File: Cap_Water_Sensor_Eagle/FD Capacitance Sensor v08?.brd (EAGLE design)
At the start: 35.1 x 27.6 mm, 17 parts, among them U1 NTS4101PT1, U2 TLC555CD

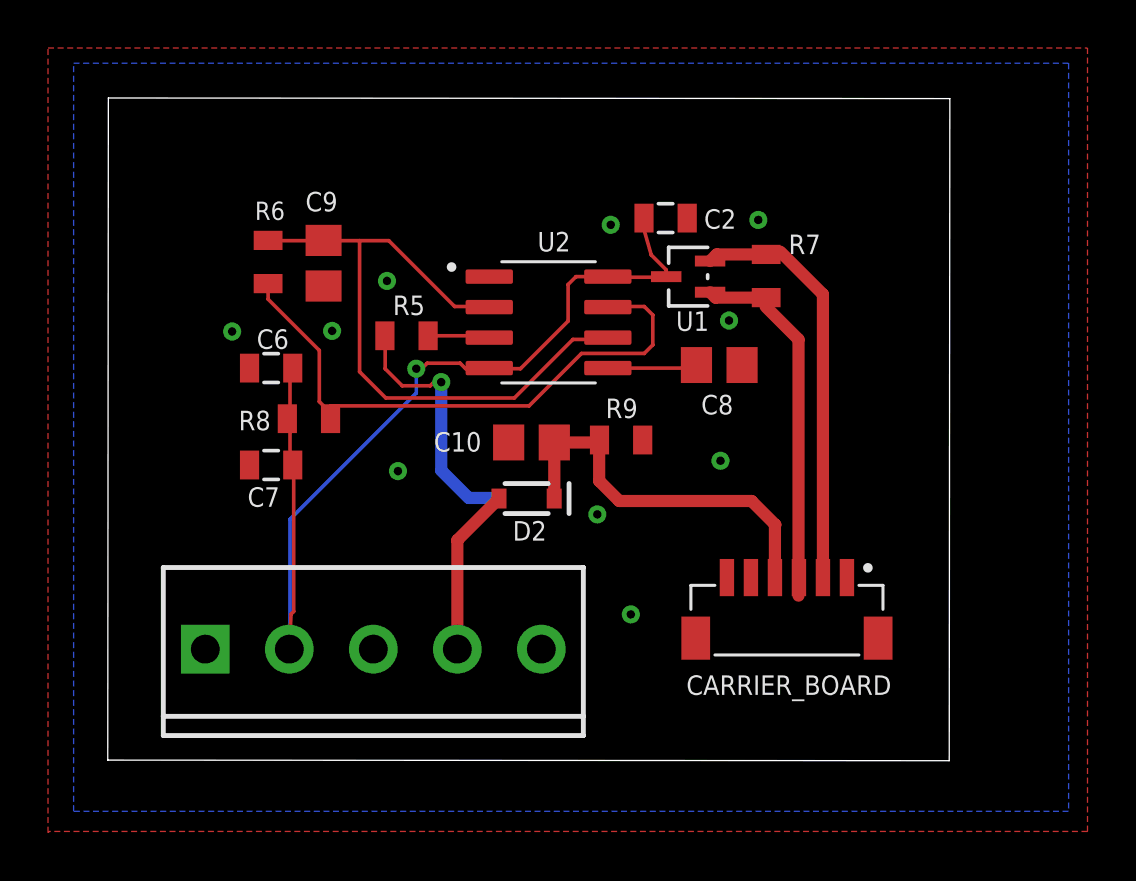
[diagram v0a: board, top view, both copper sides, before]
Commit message: Version 9 with board dimensions
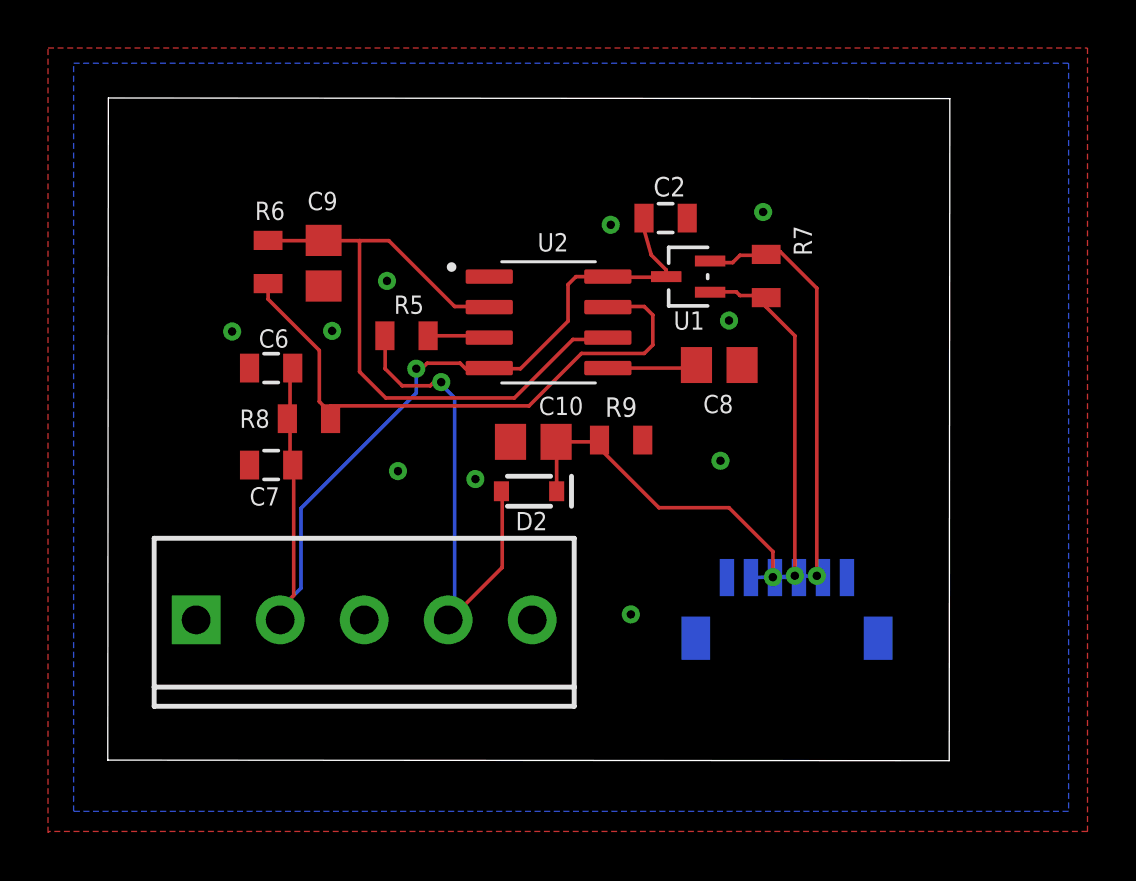
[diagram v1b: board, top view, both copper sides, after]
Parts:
- moved J1 1.28 mm to (3.68, 5.84)
- moved D2 0.32 mm to (17.6, 11.2)
- moved C10 0.08 mm to (17.7, 13.3)
- flipped CARRIER_BOARD to the bottom
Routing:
- net SENSOR1: track 17.6 -> 20.7 mm
- net +3V3: track 17.5 -> 20.0 mm, vias 0 -> 1
- net VCC: track 41.8 -> 40.2 mm
- net !EN: track 16.3 -> 15.4 mm, vias 0 -> 1
- net OUTPUT1: track 16.5 -> 16.3 mm, vias 0 -> 1
